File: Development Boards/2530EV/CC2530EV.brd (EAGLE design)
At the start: 62.6 x 57.5 mm, 42 parts, among them CON1 CC_DEBUGGER, IC1 CC2530, IC2 FT230XQ, IC3 TPS732XX, Q1 32MHz

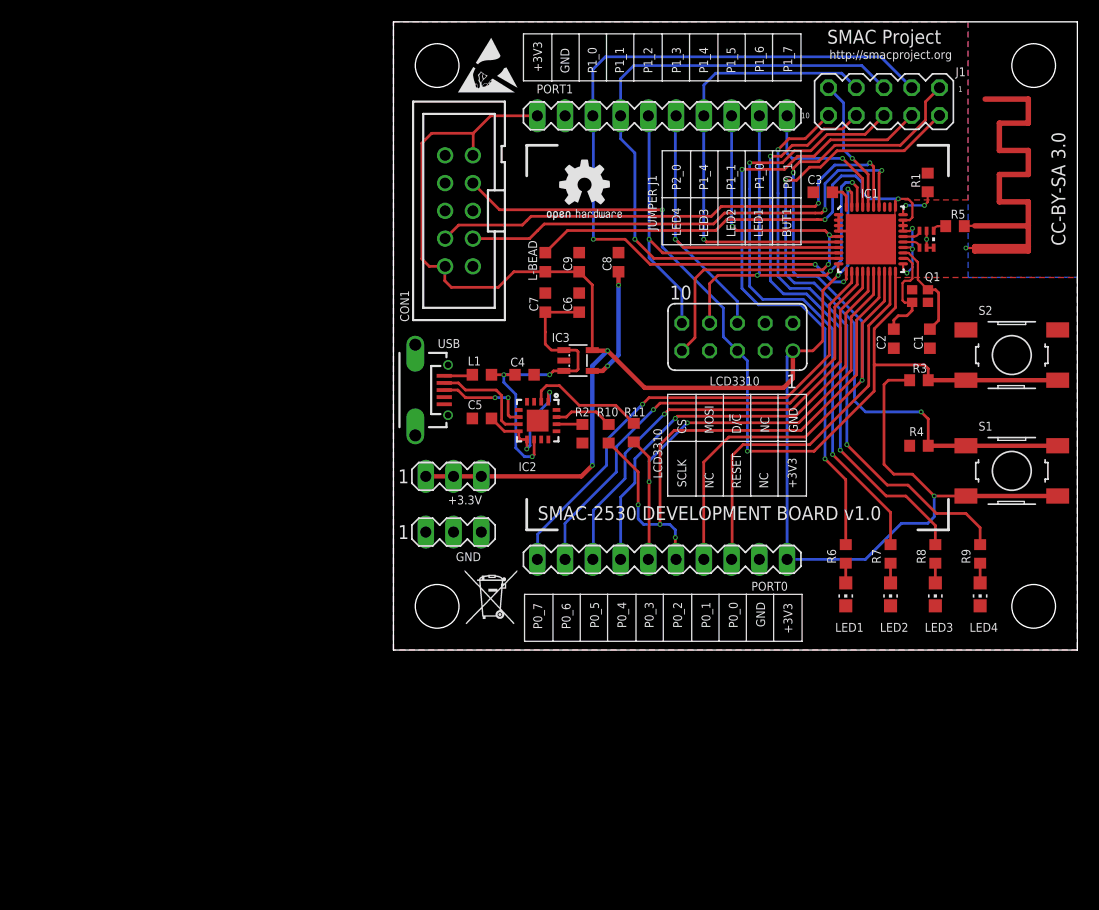
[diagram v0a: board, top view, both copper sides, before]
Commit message: Added CC2530EV reference design; added PDF schematics
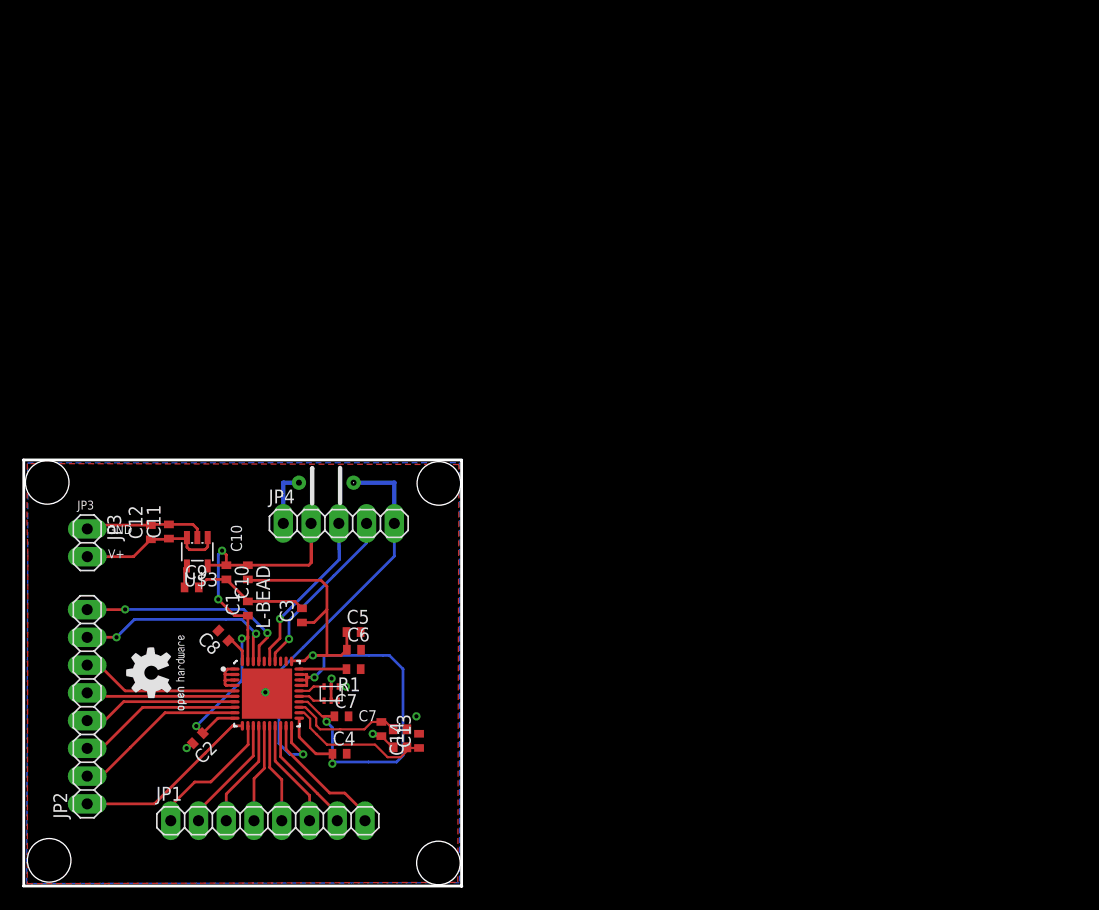
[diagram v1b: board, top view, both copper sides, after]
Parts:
- removed +3.3V, GND: (no value), con-lstb:MA03-1
- removed B1: 2450BM15A0002SLIM, johanson-technology:2450BM15A0002-SLIM
- removed CON1: CC_DEBUGGER, con-3m:PAK100/2500-10
- removed IC1: CC2530, chipcon-ti-v2:QFN50P600X600X100-41N
- removed IC2: FT230XQ, ftdichip:QFN16
- removed IC3: TPS732XX, TPS732xx:SOT23
- removed J1: (no value), con-lstb:MA05-2
- removed L1: PTC 1A, resistor:L0603K
- removed LCD3310: (no value), con-lsta:FE05-2
- removed LED1, LED2, LED3, LED4: (no value), led:CHIP-LED0805
- removed PORT0, PORT1: (no value), con-lstb:MA10-1
- removed Q1: 32MHz, crystal:FA-128
- removed R10, R11, R2, R5: 0, resistor:R0603K
- removed R3, R4: 10k, resistor:R0603K
- removed R6, R7, R8, R9: 470, resistor:R0603K
- removed S1: BUTTON1, switch-alco:ALCOSWITCH-SMD
- removed S2: RESET, switch-alco:ALCOSWITCH-SMD
- removed USB: USB-MICRO-AB, con-usb-2:USB-UAB-S1
- added C10, C12: 2u2, resistor:C0402
- added C11: 100n, resistor:C0402
- added C13, C14: 27p, resistor:C0402
- added JP1, JP2: (no value), pinhead:1X08
- added JP3: (no value), pinhead:1X02
- added JP4: (no value), pinhead:1X05
- added U$1: CC2530, chipcon-ti-v2:QFN50P600X600X100-41N
- added U$2: 24530BM15A0002, 24530BM15A0002:24530BM15A0002
- added U$3: TPS732XX, TPS732xx:SOT23
- added U$4: XTAL32M, abm_osc:2.5X2X0.5
- added U$5: PUSH_BOT, push_botton:EVQ_11_TH
- C1, C2: value 27p -> 100n; device resistor:C0603K -> resistor:C0402
- C3: value 1u -> 100n; device resistor:C0603K -> resistor:C0402
- C4: value 10u -> 100n; device resistor:C0603K -> resistor:C0402
- C5, C7: device resistor:C0603K -> resistor:C0402
- C6, C9: value 2u2 -> 100n; device resistor:C0603K -> resistor:C0402
- C8: value 100n -> 1u; device resistor:C0603K -> resistor:C0402
- L-BEAD: value 40ohm 550mA -> (none); device resistor:L0603K -> L-Bead:L-BEAD
- R1: value 56k -> 56K; device resistor:R0603K -> resistor:R0402
- moved C2 73.5 mm to (-6.20, -4.47), turned to 225 degrees
- moved R1 68.9 mm to (8.05, 1.86), turned to 180 degrees
- moved C1 67.1 mm to (-1.63, 7.40), turned to 90 degrees
- moved C3 61.4 mm to (3.32, 6.77), turned to 90 degrees
- moved GOLD_ORB_SM1 55.5 mm to (-7.07, -2.07), turned to 90 degrees
- moved C8 49.8 mm to (-3.87, 4.93), turned to 135 degrees
- moved C9 46.3 mm to (-6.77, 9.34), turned to 0 degrees
- moved C7 42.2 mm to (6.94, -2.47), turned to 0 degrees
- moved L-BEAD 39.3 mm to (-1.63, 10.7), turned to 270 degrees
- moved C4 38.6 mm to (6.77, -5.89)
- moved C6 37.9 mm to (8.09, 3.62), turned to 0 degrees
- moved C5 22.8 mm to (8.05, 5.25), turned to 0 degrees
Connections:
- removed net +3V3: +3.3V.1, +3.3V.2, +3.3V.3, C9.1, CON1.2, CON1.9, IC1.10, IC1.39, IC3.5, L-BEAD.1, LCD3310.1, PORT0.1, PORT1.1, R3.2, S1.3, S1.4
- removed net +3V3A: IC1.21, IC1.24, IC1.27, IC1.28, IC1.29, IC1.31, L-BEAD.2
- removed net +5V: C4.1, C6.1, C7.1, IC2.10, IC3.1, IC3.3, L1.1
- removed net 0V: B1.2, B1.5, B1.6, C1.2, C2.2, C3.2, C4.2, C5.2, C6.2, C7.2, C8.2, C9.2, CON1.1, GND.1, GND.2, GND.3, IC1.1, IC1.2, IC1.3, IC1.4, IC1.41, IC2.13, IC2.3, IC3.2, LCD3310.2, LED1.C, LED2.C, LED3.C, LED4.C, PORT0.2, PORT1.2, R1.1, R2.1, R4.1, R5.2, S2.1, S2.2, USB.GND, USB.GND@1, USB.GND@2, USB.GND@3, USB.GND@4, USB.ID
- removed net BUTTON1: J1.2, R4.2, S1.1, S1.2
- removed net DM: IC2.7, USB.D-
- removed net DP: IC2.6, USB.D+
- removed net LCD_CS: IC1.8, LCD3310.10, PORT1.5
- removed net LCD_D/!C: IC1.7, LCD3310.6, PORT1.6
- removed net LED1: J1.4, R6.2
- removed net LED2: J1.6, R7.2
- removed net LED3: J1.8, R8.2
- removed net LED4: J1.10, R9.2
- removed net MISO: IC1.37, PORT1.10
- removed net MOSI: IC1.38, LCD3310.8, PORT1.9
- removed net N$5: IC1.30, R1.2
- removed net P0_0: IC1.19, PORT0.3
- removed net P0_1: IC1.18, J1.1, PORT0.4
- removed net P0_2: IC1.17, PORT0.5, R10.1
- removed net P0_3: IC1.16, PORT0.6, R11.1
- removed net P0_4: IC1.15, PORT0.7
- removed net P0_5: IC1.14, PORT0.8
- removed net P0_6: IC1.13, PORT0.9
- removed net P0_7: IC1.12, PORT0.10
- removed net P1_0: IC1.11, J1.3, PORT1.3
- removed net P1_1: IC1.9, J1.5, PORT1.4
- removed net P1_4: IC1.6, J1.7, PORT1.7
- removed net P2_0: IC1.36, J1.9
- removed net RFN: B1.3, IC1.26
- removed net RFP: B1.4, IC1.25
- removed net RXD: IC2.2, R11.2
- removed net SCLK: IC1.5, LCD3310.9, PORT1.8
- removed net TXD: IC2.15, R10.2
- removed net VIO: C5.1, IC2.1, IC2.8, IC2.9
- new net GND: C1.2, C10.2, C11.2, C12.2, C13.2, C14.2, C2.2, C3.2, C4.2, C5.2, C6.2, C7.2, C8.2, C9.2, JP3.1, JP4.1, R1.1, U$1.1, U$1.2, U$1.3, U$1.4, U$1.41, U$2.P$2, U$2.P$5, U$2.P$6, U$3.2, U$4.P$2, U$4.P$4, U$5.P$2
- new net N$13: JP1.5, U$1.16
- new net N$14: JP1.6, U$1.17
- new net N$15: JP1.7, U$1.18
- new net N$16: JP1.8, U$1.19
- new net N$17: JP2.1, U$1.11
- new net N$18: JP2.2, U$1.9
- new net N$19: JP2.3, U$1.8
- new net N$20: JP2.4, U$1.7
- new net N$21: JP2.5, U$1.6
- new net N$22: JP2.6, U$1.5
- new net N$23: JP2.7, U$1.38
- new net N$24: JP2.8, U$1.37
- new net TX: U$2.P$1
- new net V+: C11.1, C12.1, JP3.2, U$3.1, U$3.3
- new net VCC: C3.1, C4.1, C5.1, C6.1, C7.1, L-BEAD.2, U$1.21, U$1.24, U$1.27, U$1.28, U$1.29, U$1.31
- new net VDD: C1.1, C10.1, C2.1, JP4.2, L-BEAD.1, U$1.10, U$1.39, U$3.5
- net DBG_DC: now also JP4.4, U$1.34; no longer CON1.3, IC1.34
- net DBG_DD: now also JP4.3, U$1.35; no longer CON1.4, IC1.35
- net N$1: now also C8.1, U$1.40; no longer C3.1, IC1.40
- net N$10: now also JP1.2, U$1.13; no longer LED2.A, R7.1
- net N$11: now also JP1.3, U$1.14; no longer LED3.A, R8.1
- net N$12: now also JP1.4, U$1.15; no longer LED4.A, R9.1
- net N$2: now also R1.2, U$1.30; no longer L1.2, USB.VBUS
- net N$3: now also U$1.25, U$2.P$4; no longer C2.1, IC1.22, Q1.3
- net N$4: now also U$1.26, U$2.P$3; no longer C1.1, IC1.23, Q1.1
- net N$6: now also C9.1, U$3.4; no longer B1.1, R5.1
- net N$7: now also C14.1, U$1.23, U$4.P$1; no longer IC2.14, R2.2
- net N$8: now also C13.1, U$1.22, U$4.P$3; no longer C8.1, IC3.4
- net N$9: now also JP1.1, U$1.12; no longer LED1.A, R6.1
- net RESET: now also JP4.5, U$1.20, U$5.P$1; no longer CON1.7, IC1.20, LCD3310.5, R3.1, S2.3, S2.4
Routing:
- net +3V3: track 182.2 -> 0.00 mm, vias 5 -> 0
- net P0_1: track 77.8 -> 0.00 mm, vias 2 -> 0
- net P1_0: track 72.0 -> 0.00 mm, vias 3 -> 0
- net VCC: track 0.00 -> 69.9 mm, vias 0 -> 4
- net BUTTON1: track 62.1 -> 0.00 mm, vias 2 -> 0
- net P1_1: track 60.1 -> 0.00 mm, vias 1 -> 0
- net LED1: track 58.2 -> 0.00 mm, vias 2 -> 0
- net LED2: track 56.6 -> 0.00 mm, vias 2 -> 0
- net LED3: track 53.5 -> 0.00 mm, vias 2 -> 0
- net LED4: track 53.5 -> 0.00 mm, vias 2 -> 0
- net P0_2: track 52.9 -> 0.00 mm, vias 3 -> 0
- net 0V: track 52.4 -> 0.00 mm, vias 2 -> 0
- net +3V3A: track 50.8 -> 0.00 mm, vias 5 -> 0
- net RESET: track 87.3 -> 38.2 mm, vias 2 -> 1
- net P0_7: track 45.7 -> 0.00 mm, vias 1 -> 0
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- added copper zone on layer 1, net GND
- added copper zone on layer 16, net GND
- removed copper zone on layer 1, net 0V
- removed copper zone on layer 16, net 0V
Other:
- board size 62.6 x 57.5 mm -> 40.2 x 39 mm
- board text added: "C1"
- board text added: "C10"
- board text added: "C11"
- board text added: "C12"
- board text added: "C13"
- board text added: "C14"
- board text added: "C2"
- board text added: "C3"
- board text added: "C4"
- board text added: "C5"
- board text added: "C6"
- board text added: "C7"
- board text added: "C8"
- board text added: "C9"
- board text added: "CC2530EV STORM LAB"
- board text added: "DBG-DC"
- board text added: "DBG-DD"
- board text added: "JP1"
- board text added: "JP2"
- board text added: "JP3"
- board text added: "JP4"
- board text added: "L"
- board text added: "R1"
- board text added: "RESET_BTN"
- board text added: "RST"
- board text added: "U2"
- board text added: "U3"
- board text added: "U4"
- board text added: "V+"
- board text added: "VDD"
- board text removed: "+3V3"
- board text removed: "BUT1"
- board text removed: "CS"
- board text removed: "D/!C"
- board text removed: "JUMPER J1"
- board text removed: "LCD3310"
- board text removed: "LED1"
- board text removed: "LED2"
- board text removed: "LED3"
- board text removed: "LED4"
- board text removed: "MOSI"
- board text removed: "NC"
- board text removed: "P2_0"
- board text removed: "RESET"
- board text removed: "SCLK"
- board text removed: "SMAC Project"
- board text removed: "SMAC-2530 DEVELOPMENT BOARD v1.0"
- board text removed: "http://smacproject.org"
